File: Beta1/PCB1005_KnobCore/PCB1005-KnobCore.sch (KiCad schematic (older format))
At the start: 34 parts, among them J1 Axoloti_40Pin, U10 OLED_128x32_I2C, U1000 MCP3008T-I/SL, U2 MCP3008T-I/SL, U20 OLED_128x32_I2C, U30 OLED_128x32_I2C, U5 I2C_1x4MUX_TCA9546A

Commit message: Added CYA TH for I2C3. Cleaned up Silkscreen.
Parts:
- added I2C_SCL3, I2C_SDA3: CONN_01X01, Liberry:single_0.1, symbol CONN_01X01
- renumbered RV_VOL to RV_VOL1
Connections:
- wire segments 197 -> 199

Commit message: First pass layout
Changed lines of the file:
@@
 JOY_3_1
 Text Label 13850 9900 0    60   ~ 0
-JOY_2_SW
+JOY_3_SW
 Wire Wire Line
 	12600 8850 12300 8850

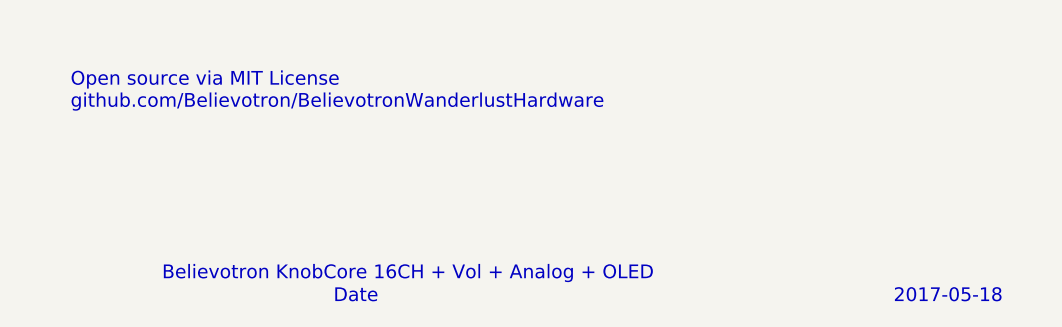
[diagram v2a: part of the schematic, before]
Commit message: Reversed OLED connectors. Ready for fab.
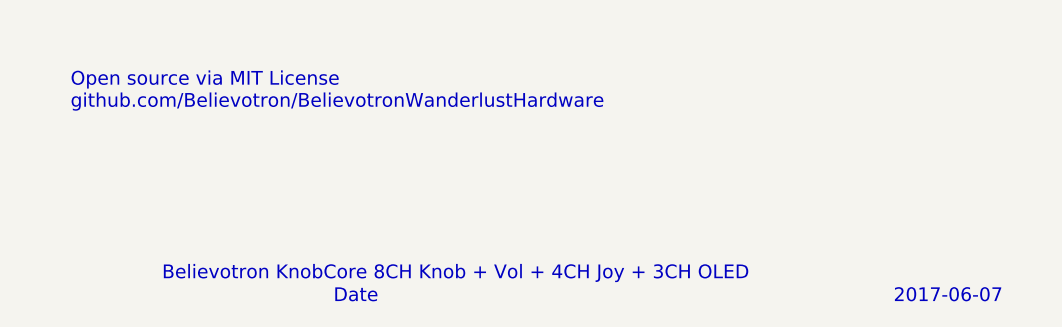
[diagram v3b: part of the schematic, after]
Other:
- note added: "2017-06-07"
- note added: "Believotron KnobCore 8CH Knob + Vol + 4CH Joy + 3CH OLED"
- note removed: "2017-05-18"
- note removed: "Believotron KnobCore 16CH + Vol + Analog + OLED"
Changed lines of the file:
@@
 $EndComp
 Text Notes 32900 21350 0    60   ~ 0
-2017-05-18
+2017-06-07
 Text Notes 29700 21250 0    60   ~ 0
-Believotron KnobCore 16CH + Vol + Analog + OLED
+Believotron KnobCore 8CH Knob + Vol + 4CH Joy + 3CH OLED
 Text Notes 29300 20500 0    60   ~ 0
 \nOpen source via MIT License\ngithub.com/Believotron/BelievotronWanderlustHardware

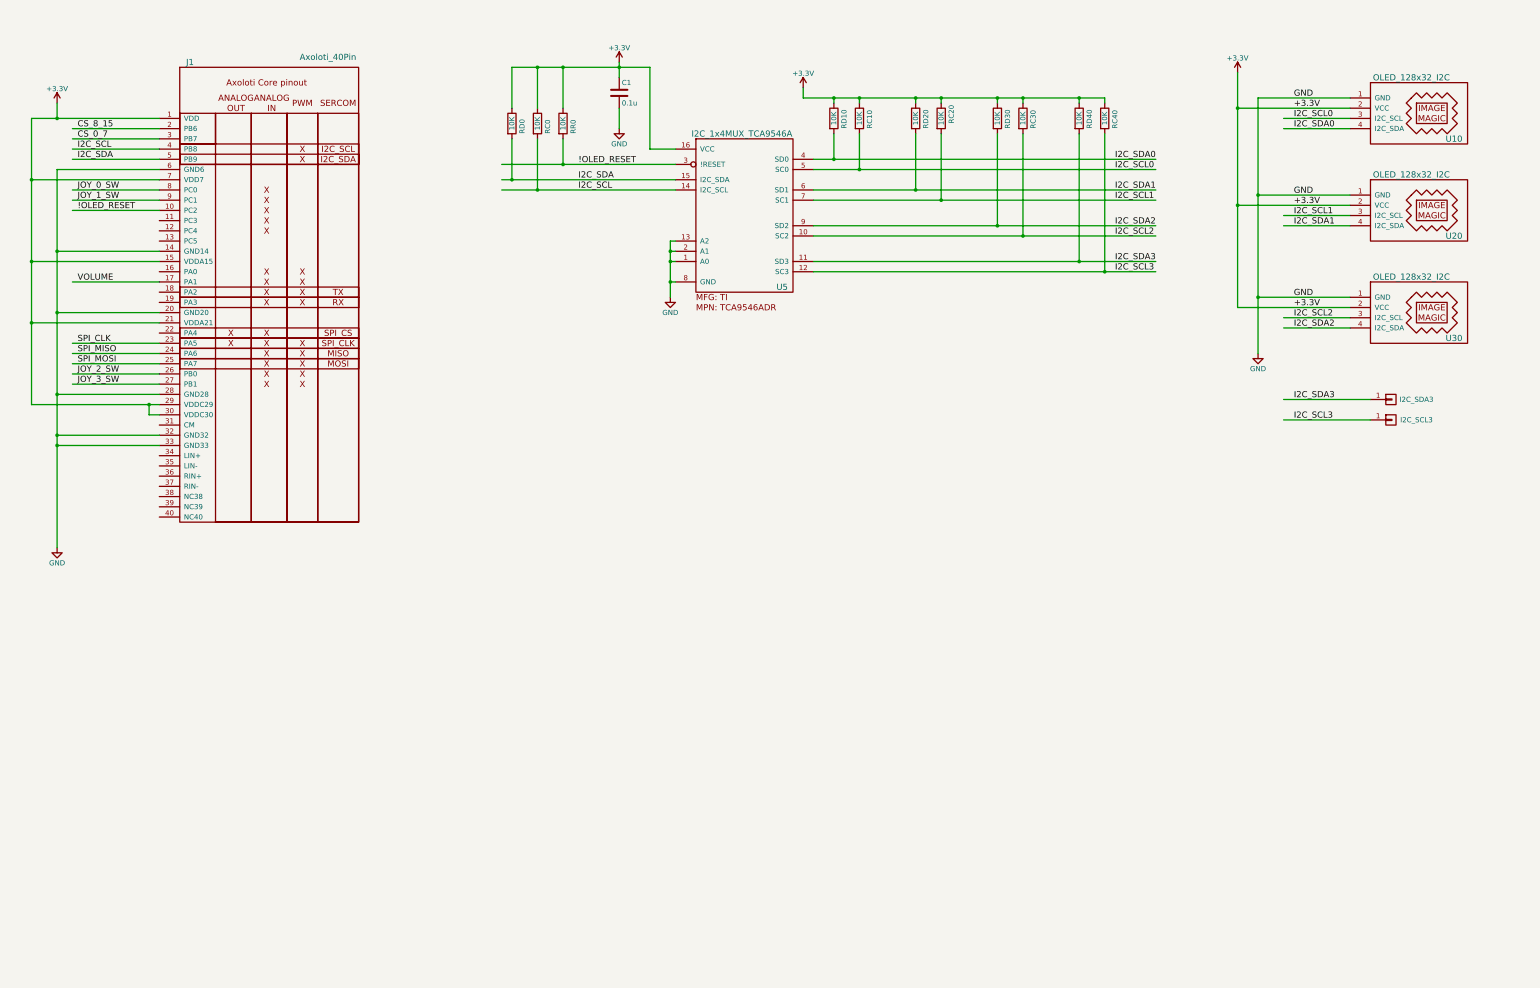
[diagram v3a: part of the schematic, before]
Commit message: Added USB-K to SCH and rough placement
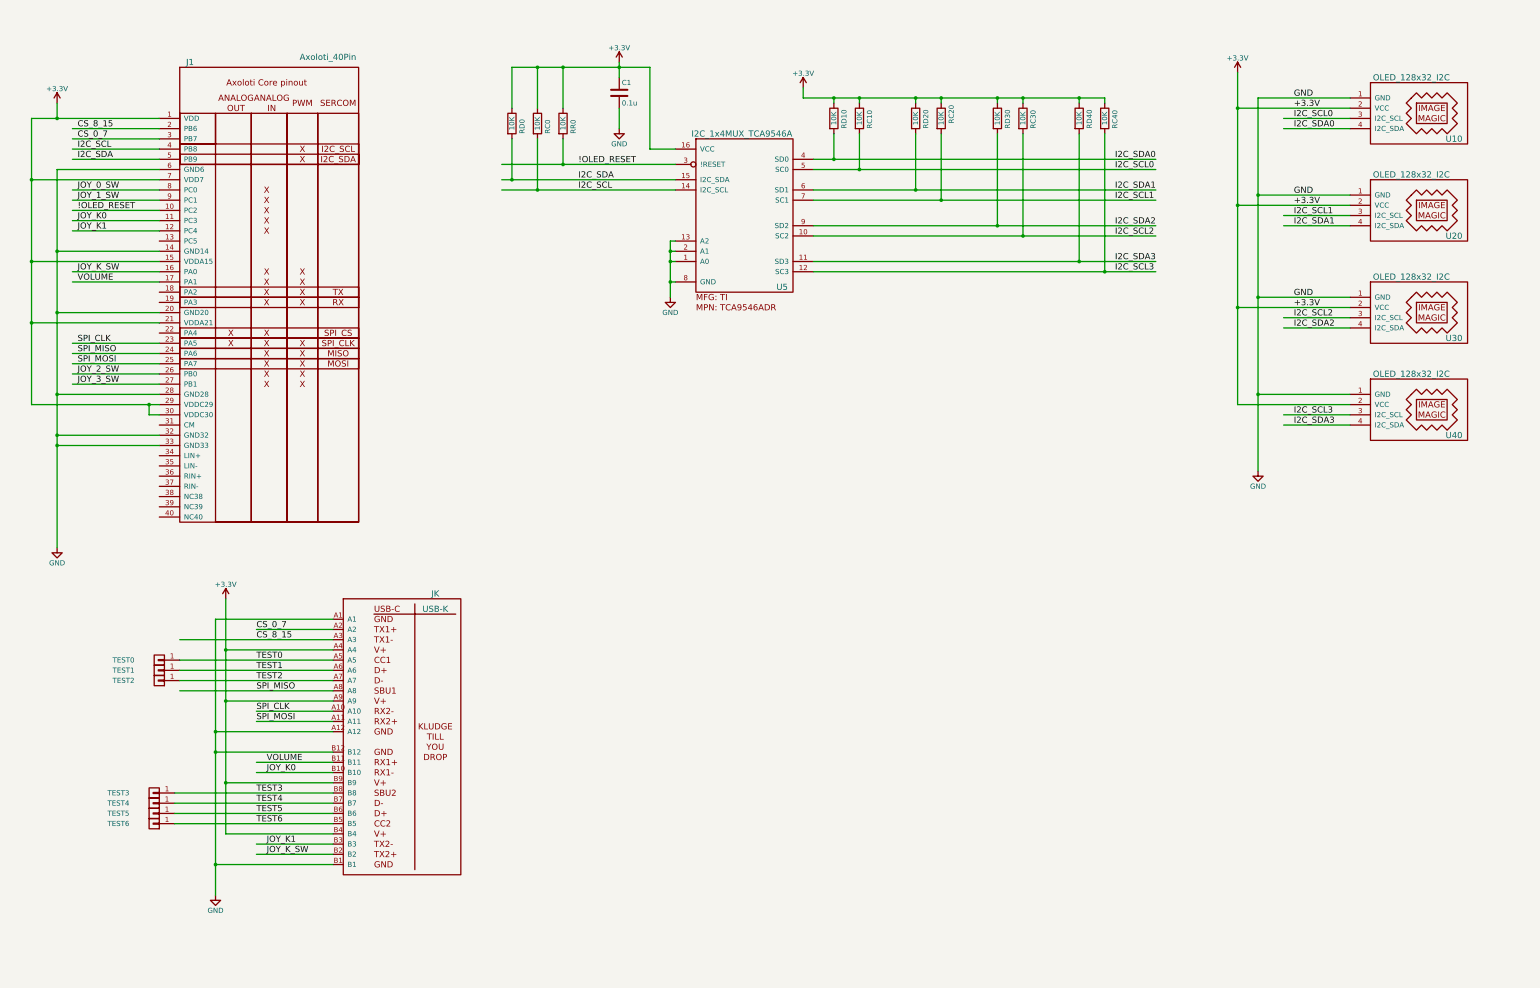
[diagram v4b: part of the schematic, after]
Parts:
- removed I2C_SCL3, I2C_SDA3: CONN_01X01, Liberry:single_0.1, symbol CONN_01X01
- added JK: USB-K, Liberry:USB-K_12401610E4_2A, symbol USB-K
- added TEST0, TEST1, TEST2, TEST3, TEST4, TEST5, TEST6: CONN_01X01, Liberry:TH_0.1_1x2_Jumper, symbol CONN_01X01
- added U40: OLED_128x32_I2C, Liberry:OLED_128x32, symbol OLED_128x32_I2C
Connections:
- net labels added: JOY_K0, JOY_K1, JOY_K_SW, TEST0, TEST1, TEST2, TEST3, TEST4, TEST5, TEST6
- wire segments 199 -> 230

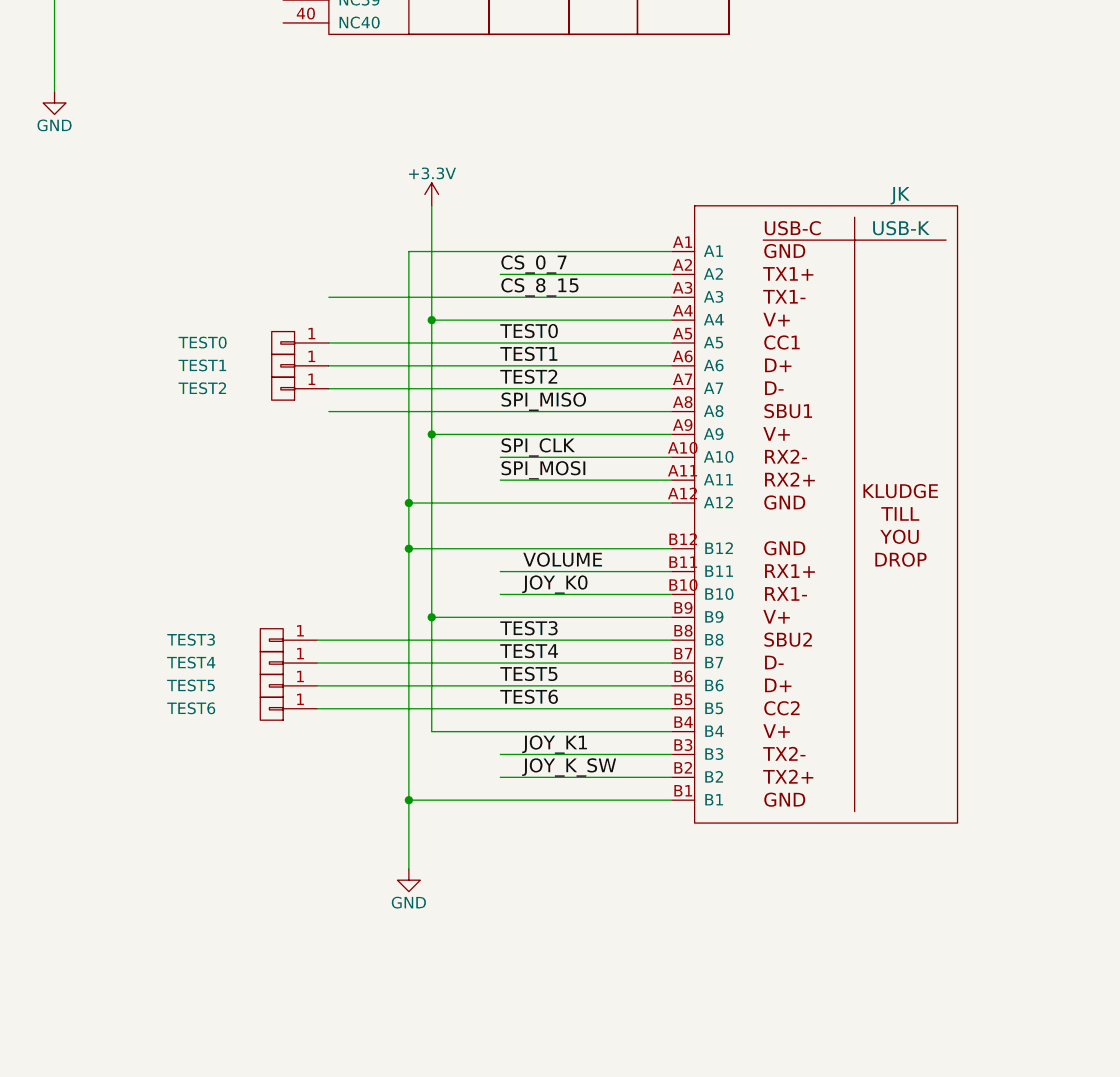
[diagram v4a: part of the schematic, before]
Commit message: Removed USB-K con, no room.
Removed USB-K from PCB1005
It's possible to fit it, but it would be a cluttered, bouncy mess.
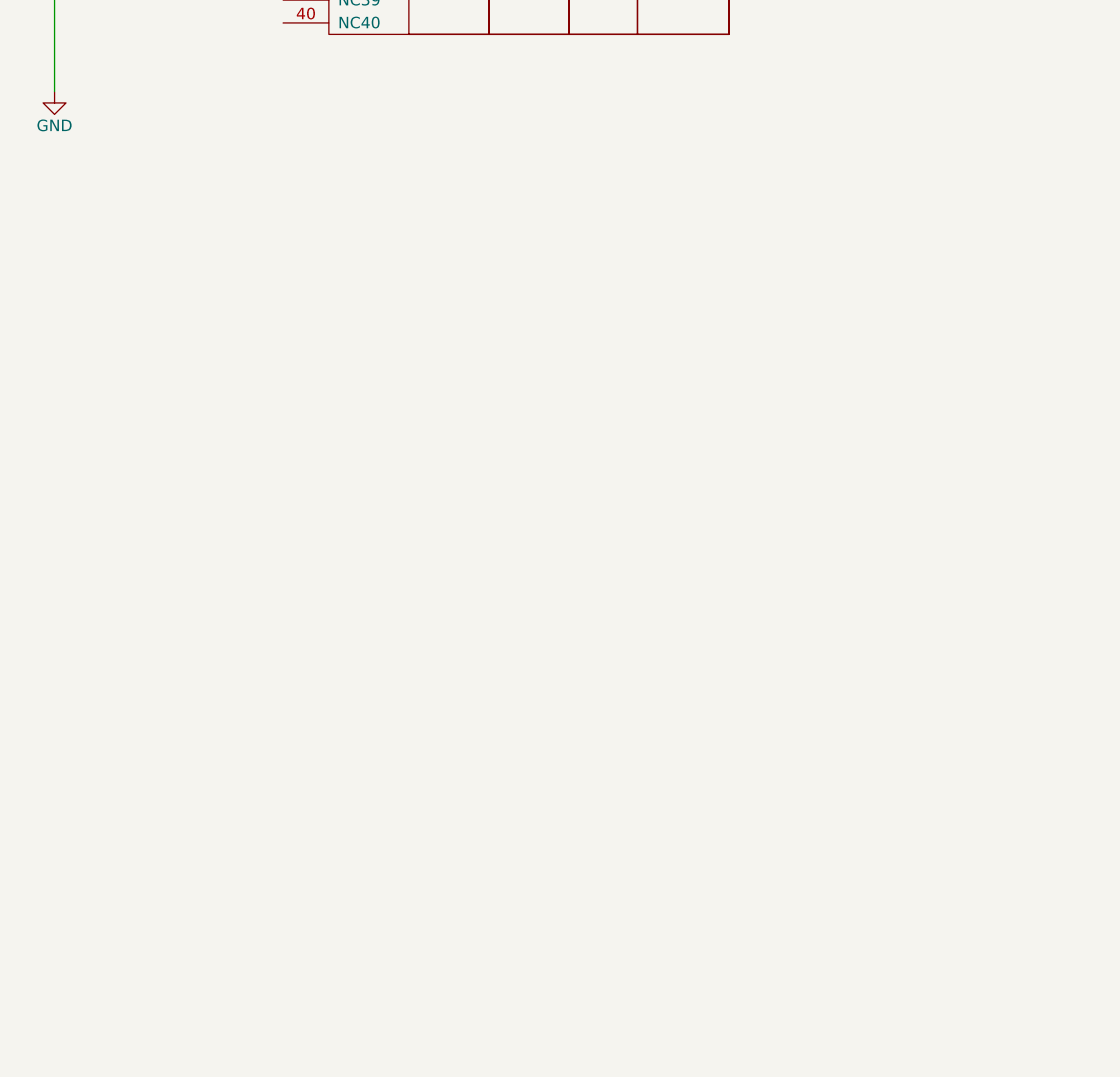
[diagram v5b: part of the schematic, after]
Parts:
- removed JK: USB-K, Liberry:USB-K_12401610E4_2A, symbol USB-K
- removed TEST0, TEST1, TEST2, TEST3, TEST4, TEST5, TEST6: CONN_01X01, Liberry:TH_0.1_1x2_Jumper, symbol CONN_01X01
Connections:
- net labels removed: TEST0, TEST1, TEST2, TEST3, TEST4, TEST5, TEST6
- wire segments 230 -> 204
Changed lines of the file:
@@
 	26450 4900 27550 4900
 Connection ~ 26450 3950
-$Comp
-L USB-K JK
-U 1 1 595813EE
-P 17600 8200
-F 0 "JK" H 18600 9650 60  0000 C CNN
-F 1 "USB-K" H 18600 9500 60  0000 C CNN
-F 2 "Liberry:USB-K_12401610E4_2A" H 17650 8100 60  0001 C CNN
-F 3 "" H 17650 8100 60  0001 C CNN
-	1    17600 8200
-	1    0    0    -1
-$EndComp
-$Comp
-L GND #PWR35
-U 1 1 595813F5
-P 16450 9700
-F 0 "#PWR35" H 16450 9450 50  0001 C CNN
-F 1 "GND" H 16450 9550 50  0000 C CNN
-F 2 "" H 16450 9700 50  0000 C CNN
-F 3 "" H 16450 9700 50  0000 C CNN
-	1    16450 9700
-	1    0    0    -1
-$EndComp
-$Comp
-L +3.3V #PWR36
-U 1 1 595813FB
-P 16550 6800
-F 0 "#PWR36" H 16550 6650 50  0001 C CNN
-F 1 "+3.3V" H 16550 6940 50  0000 C CNN
-F 2 "" H 16550 6800 50  0000 C CNN
-F 3 "" H 16550 6800 50  0000 C CNN
-	1    16550 6800
-	1    0    0    -1
-$EndComp
-Wire Wire Line
-	16450 9400 17600 9400
-Wire Wire Line
-	16450 7000 16450 9700
-Wire Wire Line
-	17600 8300 16450 8300
-Connection ~ 16450 9400
-Wire Wire Line
-	17600 8100 16450 8100
-Connection ~ 16450 8300
-Wire Wire Line
-	17600 7000 16450 7000
-Connection ~ 16450 8100
-Wire Wire Line
-	17600 7300 16550 7300
-Wire Wire Line
-	16550 6800 16550 9100
-Wire Wire Line
-	16550 7800 17600 7800
-Connection ~ 16550 7300
-Wire Wire Line
-	16550 8600 17600 8600
-Connection ~ 16550 7800
-Wire Wire Line
-	16550 9100 17600 9100
-Connection ~ 16550 8600
-Wire Wire Line
-	17600 8000 16850 8000
-Wire Wire Line
-	17600 7900 16850 7900
-Wire Wire Line
-	16100 7700 17600 7700
-Wire Wire Line
-	16100 7600 17600 7600
-Wire Wire Line
-	16100 7500 17600 7500
-Wire Wire Line
-	16100 7400 17600 7400
-Wire Wire Line
-	16100 7200 17600 7200
-Wire Wire Line
-	17600 7100 16850 7100
-Wire Wire Line
-	17600 8400 16850 8400
-Wire Wire Line
-	17600 8500 16850 8500
-Wire Wire Line
-	16050 8700 17600 8700
-Wire Wire Line
-	16050 8800 17600 8800
-Wire Wire Line
-	16050 8900 17600 8900
-Wire Wire Line
-	16050 9000 17600 9000
-Wire Wire Line
-	17600 9200 16850 9200
-Wire Wire Line
-	17600 9300 16850 9300
-Text Label 16850 8000 0    60   ~ 0
-SPI_MOSI
-Text Label 16850 7900 0    60   ~ 0
-SPI_CLK
-Text Label 16850 7100 0    60   ~ 0
-CS_0_7
-$Comp
-L CONN_01X01 TEST0
-U 1 1 59581438
-P 15900 7400
-F 0 "TEST0" H 16250 7400 50  0000 C CNN
-F 1 "CONN_01X01" V 16000 7400 50  0001 C CNN
-F 2 "Liberry:TH_0.1_1x2_Jumper" H 15900 7400 50  0001 C CNN
-F 3 "" H 15900 7400 50  0000 C CNN
-F 4 "PCB" H 15900 7400 60  0001 C CNN "MFG"
-F 5 "ON_PCB" H 15900 7400 60  0001 C CNN "MPN"
-	1    15900 7400
-	-1   0    0    1
-$EndComp
-$Comp
-L CONN_01X01 TEST1
-U 1 1 59581441
-P 15900 7500
-F 0 "TEST1" H 16250 7500 50  0000 C CNN
-F 1 "CONN_01X01" V 16000 7500 50  0001 C CNN
-F 2 "Liberry:TH_0.1_1x2_Jumper" H 15900 7500 50  0001 C CNN
-F 3 "" H 15900 7500 50  0000 C CNN
-F 4 "PCB" H 15900 7500 60  0001 C CNN "MFG"
-F 5 "ON_PCB" H 15900 7500 60  0001 C CNN "MPN"
-	1    15900 7500
-	-1   0    0    1
-$EndComp
-$Comp
-L CONN_01X01 TEST2
-U 1 1 5958144A
-P 15900 7600
-F 0 "TEST2" H 16250 7600 50  0000 C CNN
-F 1 "CONN_01X01" V 16000 7600 50  0001 C CNN
-F 2 "Liberry:TH_0.1_1x2_Jumper" H 15900 7600 50  0001 C CNN
-F 3 "" H 15900 7600 50  0000 C CNN
-F 4 "PCB" H 15900 7600 60  0001 C CNN "MFG"
-F 5 "ON_PCB" H 15900 7600 60  0001 C CNN "MPN"
-	1    15900 7600
-	-1   0    0    1
-$EndComp
-Text Label 16950 8400 0    60   ~ 0
-VOLUME
-Text Label 16950 8500 0    60   ~ 0
-JOY_K0
-Text Label 16950 9300 0    60   ~ 0
-JOY_K_SW
-Text Label 16950 9200 0    60   ~ 0
-JOY_K1
-$Comp
-L CONN_01X01 TEST3
-U 1 1 59581457
-P 15850 8700
-F 0 "TEST3" H 16200 8700 50  0000 C CNN
-F 1 "CONN_01X01" V 15950 8700 50  0001 C CNN
-F 2 "Liberry:TH_0.1_1x2_Jumper" H 15850 8700 50  0001 C CNN
-F 3 "" H 15850 8700 50  0000 C CNN
-F 4 "PCB" H 15850 8700 60  0001 C CNN "MFG"
-F 5 "ON_PCB" H 15850 8700 60  0001 C CNN "MPN"
-	1    15850 8700
-	-1   0    0    1
-$EndComp
-$Comp
-L CONN_01X01 TEST4
-U 1 1 59581460
-P 15850 8800
-F 0 "TEST4" H 16200 8800 50  0000 C CNN
-F 1 "CONN_01X01" V 15950 8800 50  0001 C CNN
-F 2 "Liberry:TH_0.1_1x2_Jumper" H 15850 8800 50  0001 C CNN
-F 3 "" H 15850 8800 50  0000 C CNN
-F 4 "PCB" H 15850 8800 60  0001 C CNN "MFG"
-F 5 "ON_PCB" H 15850 8800 60  0001 C CNN "MPN"
-	1    15850 8800
-	-1   0    0    1
-$EndComp
-$Comp
-L CONN_01X01 TEST5
-U 1 1 59581469
-P 15850 8900
-F 0 "TEST5" H 16200 8900 50  0000 C CNN
-F 1 "CONN_01X01" V 15950 8900 50  0001 C CNN
-F 2 "Liberry:TH_0.1_1x2_Jumper" H 15850 8900 50  0001 C CNN
-F 3 "" H 15850 8900 50  0000 C CNN
-F 4 "PCB" H 15850 8900 60  0001 C CNN "MFG"
-F 5 "ON_PCB" H 15850 8900 60  0001 C CNN "MPN"
-	1    15850 8900
-	-1   0    0    1
-$EndComp
-$Comp
-L CONN_01X01 TEST6
-U 1 1 59581472
-P 15850 9000
-F 0 "TEST6" H 16200 9000 50  0000 C CNN
-F 1 "CONN_01X01" V 15950 9000 50  0001 C CNN
-F 2 "Liberry:TH_0.1_1x2_Jumper" H 15850 9000 50  0001 C CNN
-F 3 "" H 15850 9000 50  0000 C CNN
-F 4 "PCB" H 15850 9000 60  0001 C CNN "MFG"
-F 5 "ON_PCB" H 15850 9000 60  0001 C CNN "MPN"
-	1    15850 9000
-	-1   0    0    1
-$EndComp
-Text Label 16850 8900 0    60   ~ 0
-TEST5
-Text Label 16850 9000 0    60   ~ 0
-TEST6
-Text Label 16850 8800 0    60   ~ 0
-TEST4
-Text Label 16850 8700 0    60   ~ 0
-TEST3
-Text Label 16850 7600 0    60   ~ 0
-TEST2
-Text Label 16850 7500 0    60   ~ 0
-TEST1
-Text Label 16850 7400 0    60   ~ 0
-TEST0
-Text Label 16850 7200 0    60   ~ 0
-CS_8_15
-Text Label 16850 7700 0    60   ~ 0
-SPI_MISO
 Text Label 15100 3100 0    60   ~ 0
 JOY_K0

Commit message: High speed signals routed
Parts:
- removed JOY0, JOY1, JOY2, JOY3: XYJOY, Liberry:XY_JOY_254TA103B50B, symbol XYJOY
- removed RV_VOL1: POT, Liberry:RV09AF-40-20K-B10K, symbol POT
- added JOY0, JOY1, JOY2, JOY3: XYJOY_Alps, Liberry:JOY_ALPS_RKJXV1224005, symbol XYJOY_Alps
- J1: footprint Liberry:Axoloti-40x2_slim -> Liberry:Axoloti-40x1_slim
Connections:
- wire segments 204 -> 201
